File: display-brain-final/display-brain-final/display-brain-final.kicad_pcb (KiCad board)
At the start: 2 copper layers, 53 x 67.1 mm, 15 parts, among them J2 Conn_01x05_Socket, J3 Conn_01x19_Socket, J4 Conn_01x19_Socket, J5 Conn_01x04_Socket, J6 Conn_01x07_Socket, J7 Conn_01x02_Socket, P1 USB_C_Plug_USB2.0, U3 AMS1117CD-3.3

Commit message: display brain platine fertig
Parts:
- added C1: 10u, Capacitor_SMD:C_1206_3216Metric_Pad1.33x1.80mm_HandSolder, F.Cu at (148.8, 83.5)
- added C2: 1u, Capacitor_SMD:C_1206_3216Metric_Pad1.33x1.80mm_HandSolder, F.Cu at (145.5, 83.5)
- added C3: 1u, Capacitor_SMD:C_1206_3216Metric_Pad1.33x1.80mm_HandSolder, F.Cu at (142.2, 83.5)
- added C4: 10u, Capacitor_SMD:C_1206_3216Metric_Pad1.33x1.80mm_HandSolder, F.Cu at (138.8, 83.5)
- added D1: LED, Diode_SMD:D_1206_3216Metric_Pad1.42x1.75mm_HandSolder, F.Cu at (140.5, 91.5)
- added R2: 330, Resistor_SMD:R_1206_3216Metric_Pad1.30x1.75mm_HandSolder, F.Cu at (140.5, 88.5)
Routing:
- net /3V3: track 27.6 -> 81.6 mm
- net Net-(U3-VI): track 45.6 -> 53.1 mm
- net Net-(D1-K): track 0.00 -> 3.03 mm

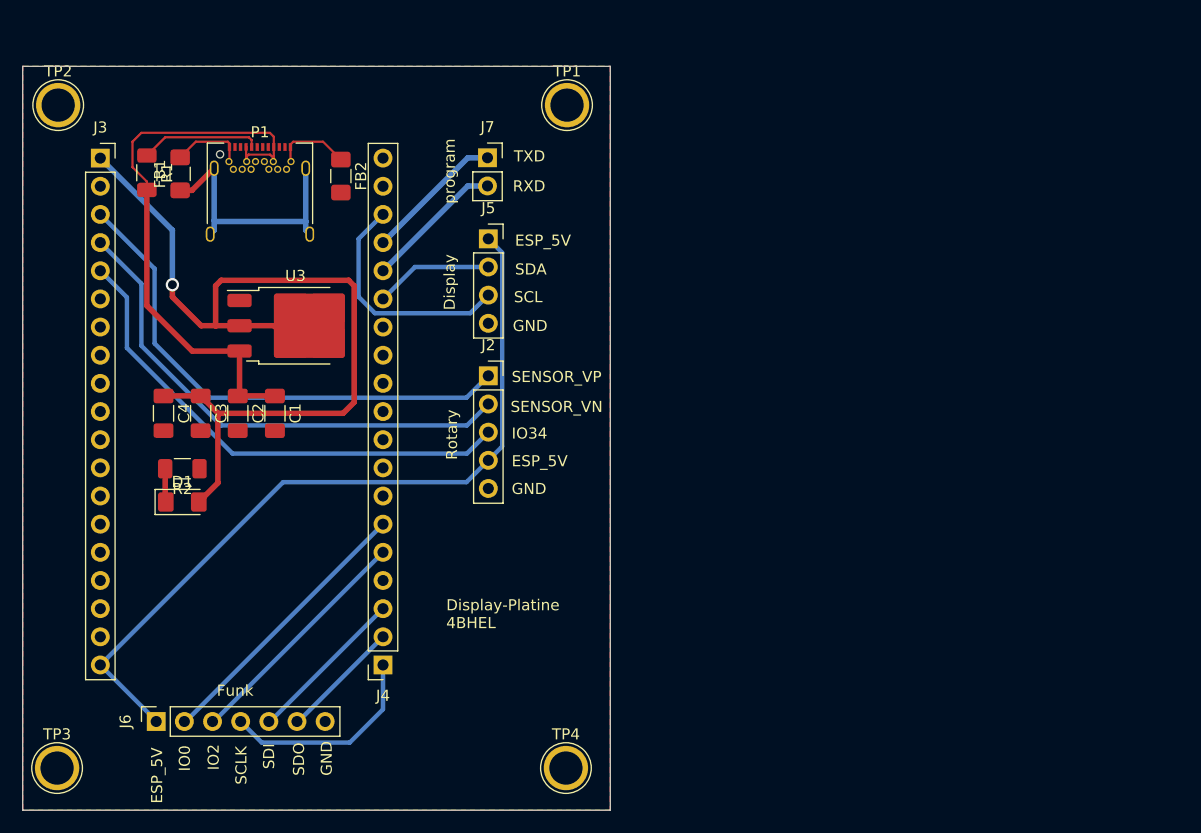
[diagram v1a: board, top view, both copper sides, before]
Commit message: display brain platine erweitert
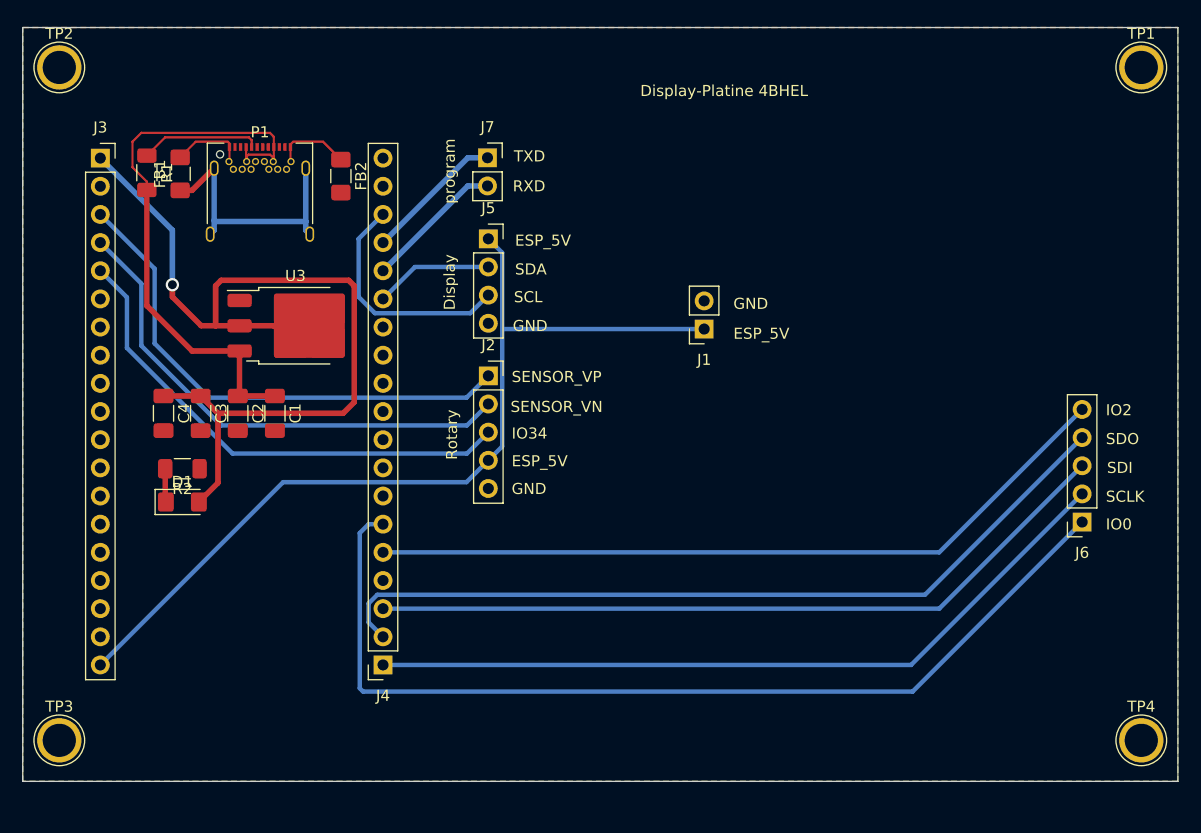
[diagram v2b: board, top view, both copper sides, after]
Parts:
- added J1: Conn_01x02_Socket, Connector_PinSocket_2.54mm:PinSocket_1x02_P2.54mm_Vertical, F.Cu at (187.6, 75.9)
- J6: value Conn_01x07_Socket -> Conn_01x05_Socket; footprint Connector_PinSocket_2.54mm:PinSocket_1x07_P2.54mm_Vertical -> Connector_PinSocket_2.54mm:PinSocket_1x05_P2.54mm_Vertical
- moved J6 85.4 mm to (221.7, 93.3), turned to 180 degrees
- moved TP4 52.0 mm to (227.0, 113.0)
- moved TP1 51.9 mm to (227.0, 52.3)
- moved TP2 3.40 mm to (129.4, 52.3)
- moved TP3 2.51 mm to (129.4, 113.0)
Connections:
- J6 pad 1: /ESP_5V -> /IO0
- J6 pad 2: /IO0 -> /CLK
- J6 pad 3: /IO2 -> /SD1
- J6 pad 4: /CLK -> /SD0
- J6 pad 5: /SD1 -> /IO2
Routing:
- net /IO0: track 25.3 -> 88.5 mm
- net /SD0: track 10.9 -> 74.1 mm
- net /SD1: track 14.5 -> 69.0 mm
- net /CLK: track 18.9 -> 69.8 mm
- net /IO2: track 21.7 -> 68.4 mm
- net /ESP_5V: track 70.8 -> 81.9 mm
- added copper zone on B.Cu, net GND
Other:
- board size 53 x 67.1 mm -> 104.2 x 68 mm
- board text removed: "Funk"

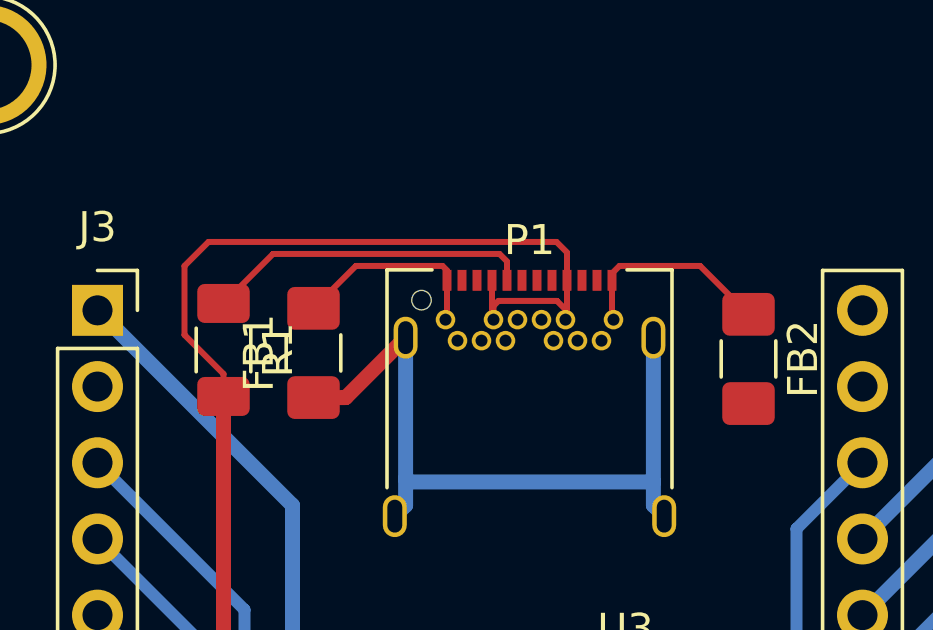
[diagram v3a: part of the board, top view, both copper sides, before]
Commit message: Increased width of power tracks from 0.2mm to 0.3mm
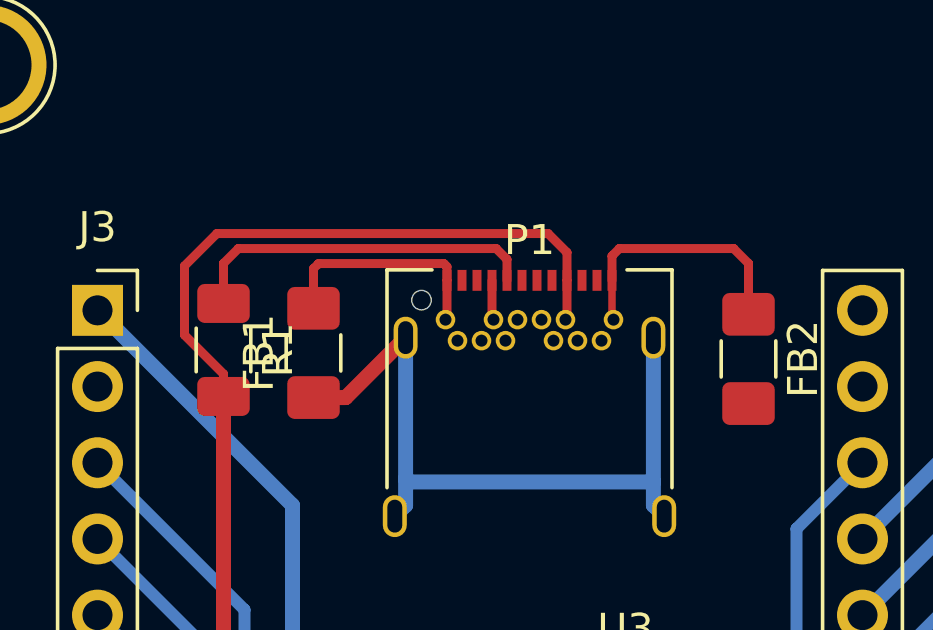
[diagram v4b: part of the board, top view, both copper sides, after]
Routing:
- net Net-(U3-VI): track 53.1 -> 49.9 mm
- net Net-(FB1-Pad2): track 13.6 -> 16.4 mm
- net Net-(P1-CC): track 10.9 -> 11.8 mm
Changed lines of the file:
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@@
   (segment (start 151.63 66.2) (end 151.63 66.98) (width 0.5) (layer "B.Cu") (net 1))
   (segment (start 143.37 66.98) (end 143.01 67.34) (width 0.5) (layer "B.Cu") (net 1))
-  (segment (start 141.7125 59) (end 140.3 60.4125) (width 0.2) (layer "F.Cu") (net 2))
-  (segment (start 153.1875 59) (end 154.8 60.6125) (width 0.2) (layer "F.Cu") (net 2))
-  (segment (start 144.75 59.15) (end 144.6 59) (width 0.2) (layer "F.Cu") (net 2))
-  (segment (start 144.6 59) (end 141.7125 59) (width 0.2) (layer "F.Cu") (net 2))
-  (segment (start 144.75 60.74) (end 144.7 60.79) (width 0.2) (layer "F.Cu") (net 2))
-  (segment (start 144.75 59.48) (end 144.75 59.15) (width 0.2) (layer "F.Cu") (net 2))
-  (segment (start 150.25 59.25) (end 150.5 59) (width 0.2) (layer "F.Cu") (net 2))
-  (segment (start 150.5 59) (end 153.1875 59) (width 0.2) (layer "F.Cu") (net 2))
-  (segment (start 150.25 59.48) (end 150.25 59.25) (width 0.2) (layer "F.Cu") (net 2))
-  (segment (start 144.75 59.48) (end 144.75 60.74) (width 0.2) (layer "F.Cu") (net 2))
-  (segment (start 150.25 59.48) (end 150.25 60.74) (width 0.2) (layer "F.Cu") (net 2))
-  (segment (start 150.25 60.74) (end 150.3 60.79) (width 0.2) (layer "F.Cu") (net 2))
+  (segment (start 140.47 58.92) (end 140.3 59.09) (width 0.3) (layer "F.Cu") (net 2))
+  (segment (start 140.3 59.09) (end 140.3 60.4125) (width 0.3) (layer "F.Cu") (net 2))
+  (segment (start 150.25 58.665) (end 150.495 58.42) (width 0.3) (layer "F.Cu") (net 2))
+  (segment (start 150.495 58.42) (end 154.305 58.42) (width 0.3) (layer "F.Cu") (net 2))
+  (segment (start 144.75 59.48) (end 144.75 60.74) (width 0.3) (layer "F.Cu") (net 2))
+  (segment (start 154.305 58.42) (end 154.8 58.915) (width 0.3) (layer "F.Cu") (net 2))
+  (segment (start 144.75 60.74) (end 144.7 60.79) (width 0.3) (layer "F.Cu") (net 2))
+  (segment (start 150.25 60.74) (end 150.25 59.48) (width 0.25) (layer "F.Cu") (net 2))
+  (segment (start 150.3 60.79) (end 150.25 60.74) (width 0.25) (layer "F.Cu") (net 2))
+  (segment (start 154.8 58.915) (end 154.8 60.6125) (width 0.3) (layer "F.Cu") (net 2))
+  (segment (start 144.75 59.025) (end 144.645 58.92) (width 0.3) (layer "F.Cu") (net 2))
+  (segment (start 144.75 59.48) (end 144.75 59.025) (width 0.3) (layer "F.Cu") (net 2))
+  (segment (start 144.645 58.92) (end 140.47 58.92) (width 0.3) (layer "F.Cu") (net 2))
+  (segment (start 150.25 59.48) (end 150.25 58.665) (width 0.3) (layer "F.Cu") (net 2))
   (segment (start 133.1 65.56) (end 138 70.46) (width 0.4) (layer "B.Cu") (net 4))
   (segment (start 138 77.2) (end 142.89 82.09) (width 0.4) (layer "B.Cu") (net 4))
@@
   (segment (start 158.6 65.56) (end 156.4 67.76) (width 0.4) (layer "B.Cu") (net 37))
   (segment (start 156.4 67.76) (end 156.4 73) (width 0.4) (layer "B.Cu") (net 37))
-  (segment (start 146.25 60.74) (end 146.3 60.79) (width 0.2) (layer "F.Cu") (net 39))
-  (segment (start 148.75 59.48) (end 148.75 60.3) (width 0.2) (layer "F.Cu") (net 39))
-  (segment (start 146.465381 60.165) (end 148.415 60.165) (width 0.2) (layer "F.Cu") (net 39))
+  (segment (start 148.12 57.92) (end 148.75 58.55) (width 0.3) (layer "F.Cu") (net 39))
+  (segment (start 137.3 62.6) (end 136 61.3) (width 0.3) (layer "F.Cu") (net 39))
+  (segment (start 146.25 60.74) (end 146.3 60.79) (width 0.3) (layer "F.Cu") (net 39))
+  (segment (start 148.75 58.55) (end 148.75 59.48) (width 0.3) (layer "F.Cu") (net 39))
   (segment (start 148.85 81.9375) (end 145.5 81.9375) (width 0.5) (layer "F.Cu") (net 39))
+  (segment (start 137.3 63.35) (end 137.3 62.6) (width 0.3) (layer "F.Cu") (net 39))
   (segment (start 145.66 77.88) (end 145.66 81.7775) (width 0.5) (layer "F.Cu") (net 39))
-  (segment (start 136.8 58.2) (end 148.4 58.2) (width 0.2) (layer "F.Cu") (net 39))
-  (segment (start 148.4 58.2) (end 148.75 58.55) (width 0.2) (layer "F.Cu") (net 39))
   (segment (start 137.3 73.8) (end 137.3 63.35) (width 0.5) (layer "F.Cu") (net 39))
   (segment (start 145.66 81.7775) (end 145.5 81.9375) (width 0.5) (layer "F.Cu") (net 39))
-  (segment (start 137.3 63.35) (end 137.3 62.6) (width 0.2) (layer "F.Cu") (net 39))
-  (segment (start 148.75 58.55) (end 148.75 59.48) (width 0.2) (layer "F.Cu") (net 39))
-  (segment (start 148.75 60.3) (end 148.75 60.74) (width 0.2) (layer "F.Cu") (net 39))
-  (segment (start 146.3 60.330381) (end 146.465381 60.165) (width 0.2) (layer "F.Cu") (net 39))
-  (segment (start 148.7 60.45) (end 148.7 60.79) (width 0.2) (layer "F.Cu") (net 39))
+  (segment (start 136 61.3) (end 136 59) (width 0.3) (layer "F.Cu") (net 39))
+  (segment (start 148.75 60.74) (end 148.7 60.79) (width 0.3) (layer "F.Cu") (net 39))
+  (segment (start 136 59) (end 137.08 57.92) (width 0.3) (layer "F.Cu") (net 39))
+  (segment (start 137.08 57.92) (end 148.12 57.92) (width 0.3) (layer "F.Cu") (net 39))
   (segment (start 141.38 77.88) (end 137.3 73.8) (width 0.5) (layer "F.Cu") (net 39))
-  (segment (start 136 61.3) (end 136 59) (width 0.2) (layer "F.Cu") (net 39))
   (segment (start 145.66 77.88) (end 141.38 77.88) (width 0.5) (layer "F.Cu") (net 39))
-  (segment (start 146.25 60.2) (end 146.25 60.74) (width 0.2) (layer "F.Cu") (net 39))
-  (segment (start 136 59) (end 136.8 58.2) (width 0.2) (layer "F.Cu") (net 39))
-  (segment (start 146.25 59.48) (end 146.25 60.2) (width 0.2) (layer "F.Cu") (net 39))
-  (segment (start 148.75 60.74) (end 148.7 60.79) (width 0.2) (layer "F.Cu") (net 39))
-  (segment (start 146.3 60.79) (end 146.3 60.330381) (width 0.2) (layer "F.Cu") (net 39))
-  (segment (start 137.3 62.6) (end 136 61.3) (width 0.2) (layer "F.Cu") (net 39))
-  (segment (start 148.415 60.165) (end 148.7 60.45) (width 0.2) (layer "F.Cu") (net 39))
-  (segment (start 137.3 60.25) (end 138.95 58.6) (width 0.2) (layer "F.Cu") (net 40))
-  (segment (start 138.95 58.6) (end 146.5 58.6) (width 0.2) (layer "F.Cu") (net 40))
-  (segment (start 146.5 58.6) (end 146.75 58.85) (width 0.2) (layer "F.Cu") (net 40))
-  (segment (start 146.75 58.85) (end 146.75 59.48) (width 0.2) (layer "F.Cu") (net 40))
+  (segment (start 148.75 59.48) (end 148.75 60.74) (width 0.3) (layer "F.Cu") (net 39))
+  (segment (start 146.25 59.48) (end 146.25 60.74) (width 0.3) (layer "F.Cu") (net 39))
+  (segment (start 146.75 59.48) (end 146.75 58.78) (width 0.3) (layer "F.Cu") (net 40))
+  (segment (start 146.75 58.78) (end 146.39 58.42) (width 0.3) (layer "F.Cu") (net 40))
+  (segment (start 137.795 58.42) (end 137.3 58.915) (width 0.3) (layer "F.Cu") (net 40))
+  (segment (start 146.39 58.42) (end 137.795 58.42) (width 0.3) (layer "F.Cu") (net 40))
+  (segment (start 137.3 58.915) (end 137.3 60.25) (width 0.3) (layer "F.Cu") (net 40))
   (segment (start 138.95 88.5) (end 138.95 91.4375) (width 0.5) (layer "F.Cu") (net 48))
   (segment (start 138.95 91.4375) (end 139.0125 91.5) (width 0.5) (layer "F.Cu") (net 48))

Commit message: 5v versorgung für display geändert
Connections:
- C1 pad 1: Net-(U3-VI) -> /5V
- C2 pad 1: Net-(U3-VI) -> /5V
- J1 pad 1: /ESP_5V -> /5V
- J2 pad 4: /ESP_5V -> /5V
- J5 pad 1: /ESP_5V -> /5V
- P1 pad A4: Net-(U3-VI) -> /5V
- P1 pad A9: Net-(U3-VI) -> /5V
- P1 pad B4: Net-(U3-VI) -> /5V
- P1 pad B9: Net-(U3-VI) -> /5V
- R1 pad 2: Net-(U3-VI) -> /5V
- U3 pad 3: Net-(U3-VI) -> /5V
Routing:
- net /5V: track 0.00 -> 111.4 mm, vias 0 -> 1
- net /ESP_5V: track 81.9 -> 0.00 mm
- net Net-(U3-VI): track 49.9 -> 0.00 mm
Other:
- board text added: "5V"
- board text removed: "ESP_5V"
